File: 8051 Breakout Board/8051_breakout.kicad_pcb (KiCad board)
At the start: 2 copper layers, 55.9 x 83.8 mm, 37 parts, among them J1 Conn_01x20, J2 Conn_01x20, J3 Conn_02x03_Counter_Clockwise, SW1 SW_Push_Dual, U1 AT89S51-24PU, Y1 ABL-11.0592MHZ-B1U-T

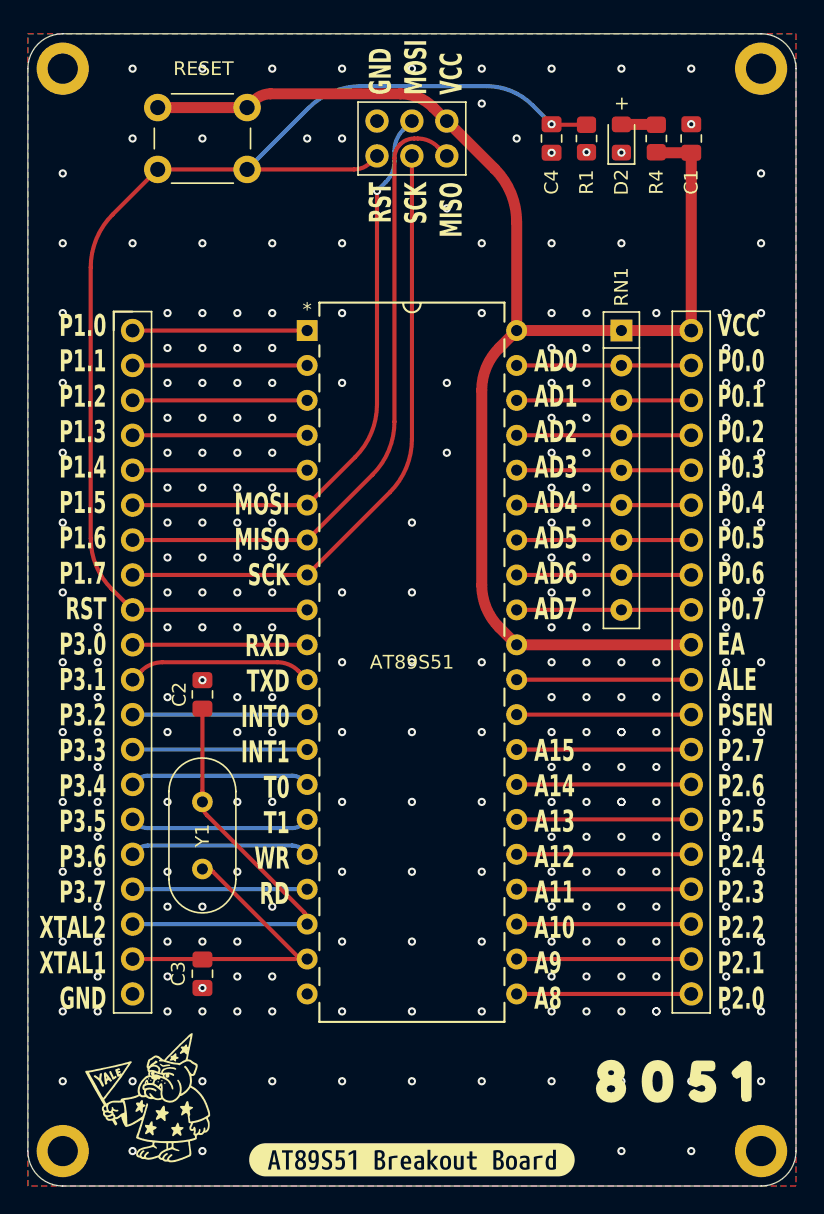
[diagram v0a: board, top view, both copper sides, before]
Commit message: 5v power plane
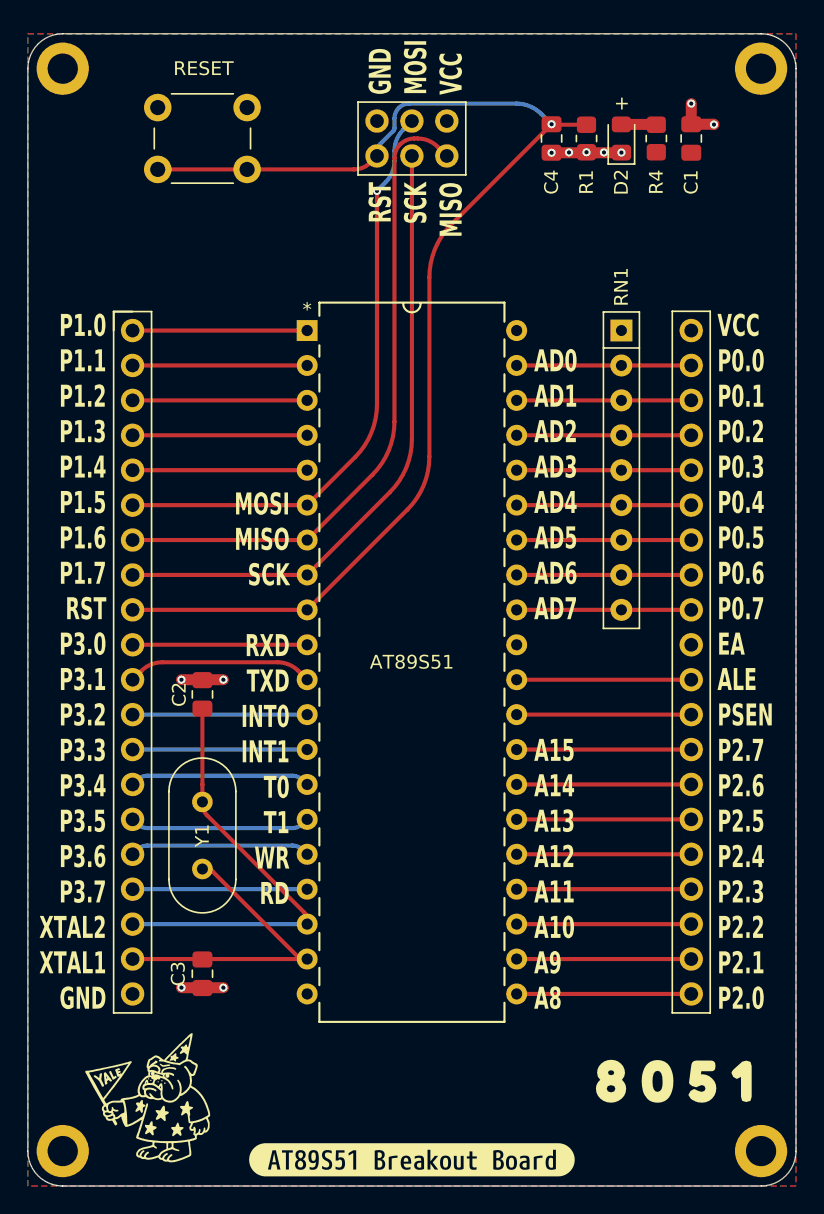
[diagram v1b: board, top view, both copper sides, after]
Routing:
- net +5V: track 104.5 -> 0.00 mm
- net GND: track 0.00 -> 14.3 mm, vias 262 -> 11
- net /RST: track 91.7 -> 89.5 mm
- added copper zone on F.Cu, net +5V
- removed copper zone on F.Cu, net GND
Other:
- board text added: "M"
- board text added: "O"

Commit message: gerber fix
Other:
- board text added: "MOMCHIL KOLEV"
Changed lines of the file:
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@@
+		)
+	)
+	(gr_text "MOMCHIL\nKOLEV"
+		(at 92.964 68.834 0)
+		(layer "F.SilkS")
+		(effects
+			(font
+				(size 1.6 1.8)
+				(thickness 0.4)
+				(bold yes)
+			)
+			(justify bottom)
 		)
 	)
